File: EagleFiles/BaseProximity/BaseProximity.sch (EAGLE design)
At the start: 22 parts, among them Q3 2N3904

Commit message: board order for v1.0
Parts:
- added Q1: 2N3904, SparkFun-DiscreteSemi:TRANSISTOR_NPN2N3904-EZ
- added R1: 1K, SparkFun-Resistors:1KOHM-1/4W-1%(PTH)HORIZ-KIT
- renumbered 5983 to COMPASS, JP7 to TO_MBOT
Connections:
- new net IR_GND2: FRONTRIGHT.2, Q1.C, REAR.2, REARRIGHT.2, RIGHT.2
- new net N$1: Q1.B, R1.1
- net GND: now also Q1.E
- net GPIO12: now also R1.2
- net IR_GND: no longer FRONTRIGHT.2, REAR.2, REARRIGHT.2, RIGHT.2
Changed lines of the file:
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@@
 <part name="GPIO5" library="pinhead" deviceset="PINHD-1X3" device=""/>
 <part name="GPIO6" library="pinhead" deviceset="PINHD-1X3" device=""/>
-<part name="5983" library="pinhead" deviceset="PINHD-1X6" device=""/>
+<part name="COMPASS" library="pinhead" deviceset="PINHD-1X6" device=""/>
 <part name="GPIO13" library="pinhead" deviceset="PINHD-1X3" device=""/>
 <part name="GPIO19" library="pinhead" deviceset="PINHD-1X3" device=""/>
-<part name="JP7" library="pinhead" deviceset="PINHD-1X4" device=""/>
+<part name="TO_MBOT" library="pinhead" deviceset="PINHD-1X4" device=""/>
 <part name="Q3" library="SparkFun-DiscreteSemi" deviceset="TRANSISTOR_NPN" device="2N3904-EZ" value="2N3904"/>
 <part name="R5" library="SparkFun-Resistors" deviceset="1KOHM-1/4W-1%(PTH)" device="HORIZ-KIT" value="1K"/>
+<part name="Q1" library="SparkFun-DiscreteSemi" deviceset="TRANSISTOR_NPN" device="2N3904-EZ" value="2N3904"/>
+<part name="R1" library="SparkFun-Resistors" deviceset="1KOHM-1/4W-1%(PTH)" device="HORIZ-KIT" value="1K"/>
 </parts>
 <sheets>
@@
 <instance part="GPIO5" gate="A" x="114.3" y="170.18"/>
 <instance part="GPIO6" gate="A" x="114.3" y="154.94"/>
-<instance part="5983" gate="A" x="124.46" y="119.38"/>
+<instance part="COMPASS" gate="A" x="124.46" y="119.38"/>
 <instance part="GPIO13" gate="A" x="142.24" y="170.18"/>
 <instance part="GPIO19" gate="A" x="142.24" y="154.94"/>
-<instance part="JP7" gate="A" x="226.06" y="165.1"/>
+<instance part="TO_MBOT" gate="A" x="226.06" y="165.1"/>
 <instance part="Q3" gate="G$1" x="134.62" y="83.82"/>
 <instance part="R5" gate="G$1" x="124.46" y="83.82" rot="R180"/>
+<instance part="Q1" gate="G$1" x="78.74" y="111.76"/>
+<instance part="R1" gate="G$1" x="68.58" y="111.76" rot="R180"/>
 </instances>
 <busses>
@@
 </segment>
 <segment>
-<pinref part="5983" gate="A" pin="5"/>
+<pinref part="COMPASS" gate="A" pin="5"/>
 <wire x1="121.92" y1="116.84" x2="109.22" y2="116.84" width="0.1524" layer="91"/>
 <label x="109.22" y="116.84" size="1.778" layer="95"/>
@@
 </segment>
 <segment>
-<pinref part="JP7" gate="A" pin="4"/>
+<pinref part="TO_MBOT" gate="A" pin="4"/>
 <wire x1="223.52" y1="162.56" x2="208.28" y2="162.56" width="0.1524" layer="91"/>
 <label x="208.28" y="162.56" size="1.778" layer="95"/>
@@
 <label x="137.16" y="76.2" size="1.778" layer="95"/>
 </segment>
+<segment>
+<wire x1="81.28" y1="104.14" x2="81.28" y2="106.68" width="0.1524" layer="91"/>
+<pinref part="Q1" gate="G$1" pin="E"/>
+<label x="81.28" y="104.14" size="1.778" layer="95"/>
+</segment>
 </net>
 <net name="VCC" class="0">
@@
 </segment>
 <segment>
-<pinref part="5983" gate="A" pin="6"/>
+<pinref part="COMPASS" gate="A" pin="6"/>
 <wire x1="121.92" y1="114.3" x2="109.22" y2="114.3" width="0.1524" layer="91"/>
 <label x="109.22" y="114.3" size="1.778" layer="95"/>
@@
 </segment>
 <segment>
-<pinref part="5983" gate="A" pin="4"/>
+<pinref part="COMPASS" gate="A" pin="4"/>
 <wire x1="121.92" y1="119.38" x2="109.22" y2="119.38" width="0.1524" layer="91"/>
 <label x="109.22" y="119.38" size="1.778" layer="95"/>
@@
 </segment>
 <segment>
-<pinref part="5983" gate="A" pin="3"/>
+<pinref part="COMPASS" gate="A" pin="3"/>
 <wire x1="121.92" y1="121.92" x2="109.22" y2="121.92" width="0.1524" layer="91"/>
 <label x="109.22" y="121.92" size="1.778" layer="95"/>
@@
 </segment>
 <segment>
-<pinref part="JP7" gate="A" pin="1"/>
+<pinref part="TO_MBOT" gate="A" pin="1"/>
 <wire x1="223.52" y1="170.18" x2="208.28" y2="170.18" width="0.1524" layer="91"/>
 <label x="208.28" y="170.18" size="1.778" layer="95"/>
@@
 <net name="N$9" class="0">
 <segment>
-<pinref part="5983" gate="A" pin="2"/>
+<pinref part="COMPASS" gate="A" pin="2"/>
 <wire x1="121.92" y1="124.46" x2="109.22" y2="124.46" width="0.1524" layer="91"/>
 </segment>
@@
 <net name="N$12" class="0">
 <segment>
-<pinref part="5983" gate="A" pin="1"/>
+<pinref part="COMPASS" gate="A" pin="1"/>
 <wire x1="121.92" y1="127" x2="109.22" y2="127" width="0.1524" layer="91"/>
 </segment>
@@
 </segment>
 <segment>
-<pinref part="JP7" gate="A" pin="2"/>
+<pinref part="TO_MBOT" gate="A" pin="2"/>
 <wire x1="223.52" y1="167.64" x2="208.28" y2="167.64" width="0.1524" layer="91"/>
 <label x="208.28" y="167.64" size="1.778" layer="95"/>
@@
 </segment>
 <segment>
-<pinref part="JP7" gate="A" pin="3"/>
+<pinref part="TO_MBOT" gate="A" pin="3"/>
 <wire x1="223.52" y1="165.1" x2="208.28" y2="165.1" width="0.1524" layer="91"/>
 <label x="208.28" y="165.1" size="1.778" layer="95"/>
@@
 <wire x1="231.14" y1="81.28" x2="241.3" y2="81.28" width="0.1524" layer="91"/>
 <label x="236.22" y="81.28" size="1.778" layer="95"/>
+</segment>
+<segment>
+<pinref part="R1" gate="G$1" pin="2"/>
+<wire x1="63.5" y1="111.76" x2="60.96" y2="111.76" width="0.1524" layer="91"/>
+<label x="60.96" y="116.84" size="1.778" layer="95"/>
 </segment>
 </net>
@@
 </segment>
 <segment>
+<pinref part="LEFT" gate="A" pin="2"/>
+<wire x1="25.4" y1="38.1" x2="15.24" y2="38.1" width="0.1524" layer="91"/>
+<label x="15.24" y="38.1" size="1.778" layer="95"/>
+</segment>
+<segment>
+<pinref part="REARLEFT" gate="A" pin="2"/>
+<wire x1="25.4" y1="20.32" x2="17.78" y2="20.32" width="0.1524" layer="91"/>
+<label x="17.78" y="20.32" size="1.778" layer="95"/>
+</segment>
+<segment>
 <pinref part="FRONT" gate="A" pin="2"/>
 <wire x1="43.18" y1="55.88" x2="35.56" y2="55.88" width="0.1524" layer="91"/>
 <label x="35.56" y="55.88" size="1.778" layer="95"/>
 </segment>
+</net>
+<net name="N$1" class="0">
+<segment>
+<wire x1="73.66" y1="111.76" x2="76.2" y2="111.76" width="0.1524" layer="91"/>
+<pinref part="Q1" gate="G$1" pin="B"/>
+<pinref part="R1" gate="G$1" pin="1"/>
+</segment>
+</net>
+<net name="IR_GND2" class="0">
+<segment>
+<pinref part="Q1" gate="G$1" pin="C"/>
+<wire x1="81.28" y1="116.84" x2="81.28" y2="124.46" width="0.1524" layer="91"/>
+<label x="81.28" y="121.92" size="1.778" layer="95"/>
+</segment>
+<segment>
+<pinref part="REARRIGHT" gate="A" pin="2"/>
+<wire x1="60.96" y1="20.32" x2="53.34" y2="20.32" width="0.1524" layer="91"/>
+<label x="53.34" y="20.32" size="1.778" layer="95"/>
+</segment>
+<segment>
+<pinref part="RIGHT" gate="A" pin="2"/>
+<wire x1="60.96" y1="38.1" x2="53.34" y2="38.1" width="0.1524" layer="91"/>
+<label x="53.34" y="38.1" size="1.778" layer="95"/>
+</segment>
 <segment>
 <pinref part="FRONTRIGHT" gate="A" pin="2"/>
@@
 </segment>
 <segment>
-<pinref part="LEFT" gate="A" pin="2"/>
-<wire x1="25.4" y1="38.1" x2="15.24" y2="38.1" width="0.1524" layer="91"/>
-<label x="15.24" y="38.1" size="1.778" layer="95"/>
-</segment>
-<segment>
-<pinref part="REARLEFT" gate="A" pin="2"/>
-<wire x1="25.4" y1="20.32" x2="17.78" y2="20.32" width="0.1524" layer="91"/>
-<label x="17.78" y="20.32" size="1.778" layer="95"/>
-</segment>
-<segment>
 <pinref part="REAR" gate="A" pin="2"/>
 <wire x1="43.18" y1="20.32" x2="35.56" y2="20.32" width="0.1524" layer="91"/>
 <label x="35.56" y="20.32" size="1.778" layer="95"/>
 </segment>
-<segment>
-<pinref part="REARRIGHT" gate="A" pin="2"/>
-<wire x1="60.96" y1="20.32" x2="53.34" y2="20.32" width="0.1524" layer="91"/>
-<label x="53.34" y="20.32" size="1.778" layer="95"/>
-</segment>
-<segment>
-<pinref part="RIGHT" gate="A" pin="2"/>
-<wire x1="60.96" y1="38.1" x2="53.34" y2="38.1" width="0.1524" layer="91"/>
-<label x="53.34" y="38.1" size="1.778" layer="95"/>
-</segment>
-</net>
+</net>

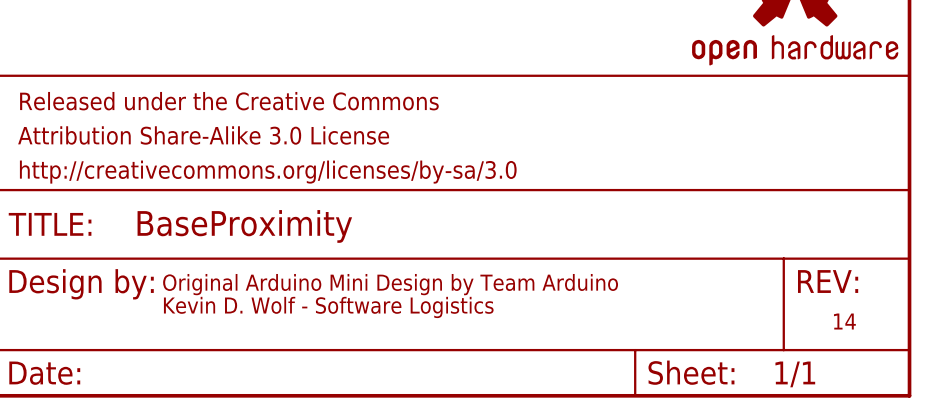
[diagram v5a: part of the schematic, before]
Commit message: update instructions for board
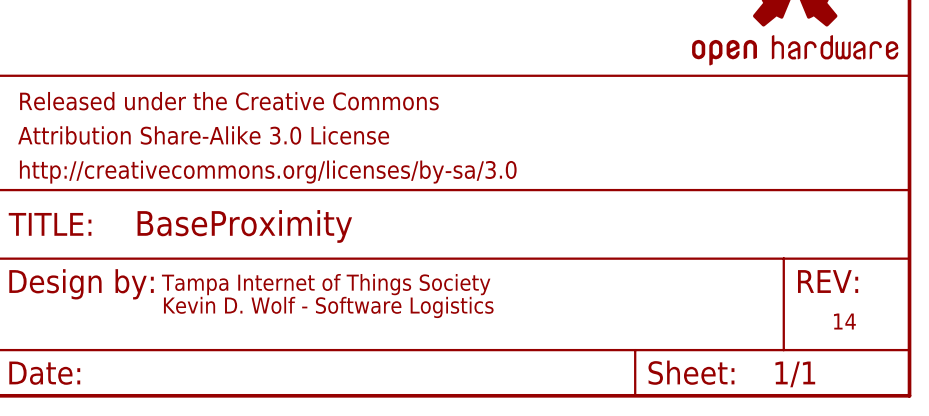
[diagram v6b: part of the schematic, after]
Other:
- note added: "Tampa Internet of Things Society"
- note removed: "Original Arduino Mini Design by Team Arduino"
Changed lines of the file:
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@@
 <sheet>
 <plain>
-<text x="165.862" y="11.684" size="1.778" layer="94">Original Arduino Mini Design by Team Arduino</text>
+<text x="165.862" y="11.684" size="1.778" layer="94">Tampa Internet of Things Society</text>
 <text x="165.862" y="9.144" size="1.778" layer="94">Kevin D. Wolf - Software Logistics</text>
 <text x="240.284" y="7.366" size="1.778" layer="94">14</text>

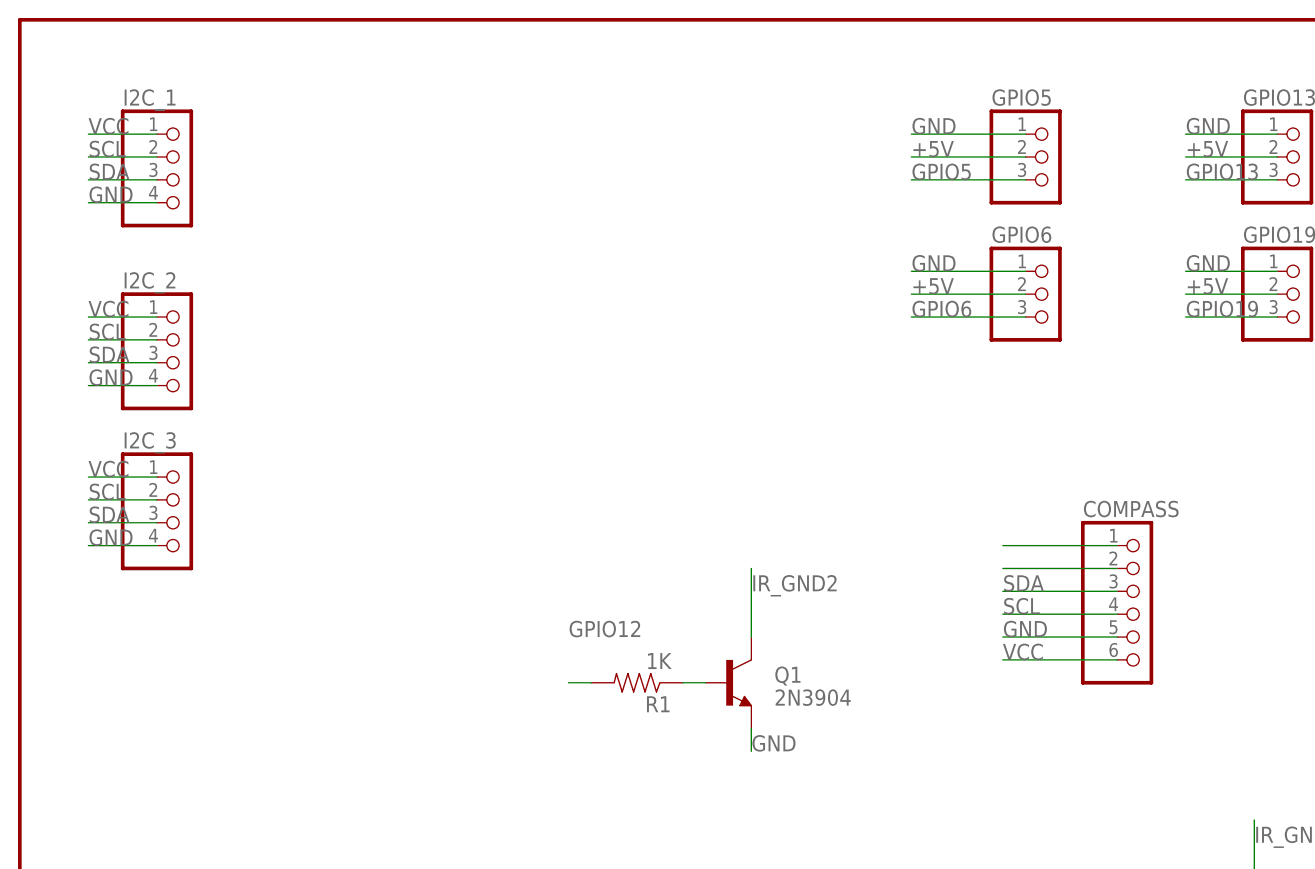
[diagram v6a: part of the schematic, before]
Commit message: updated board for new order
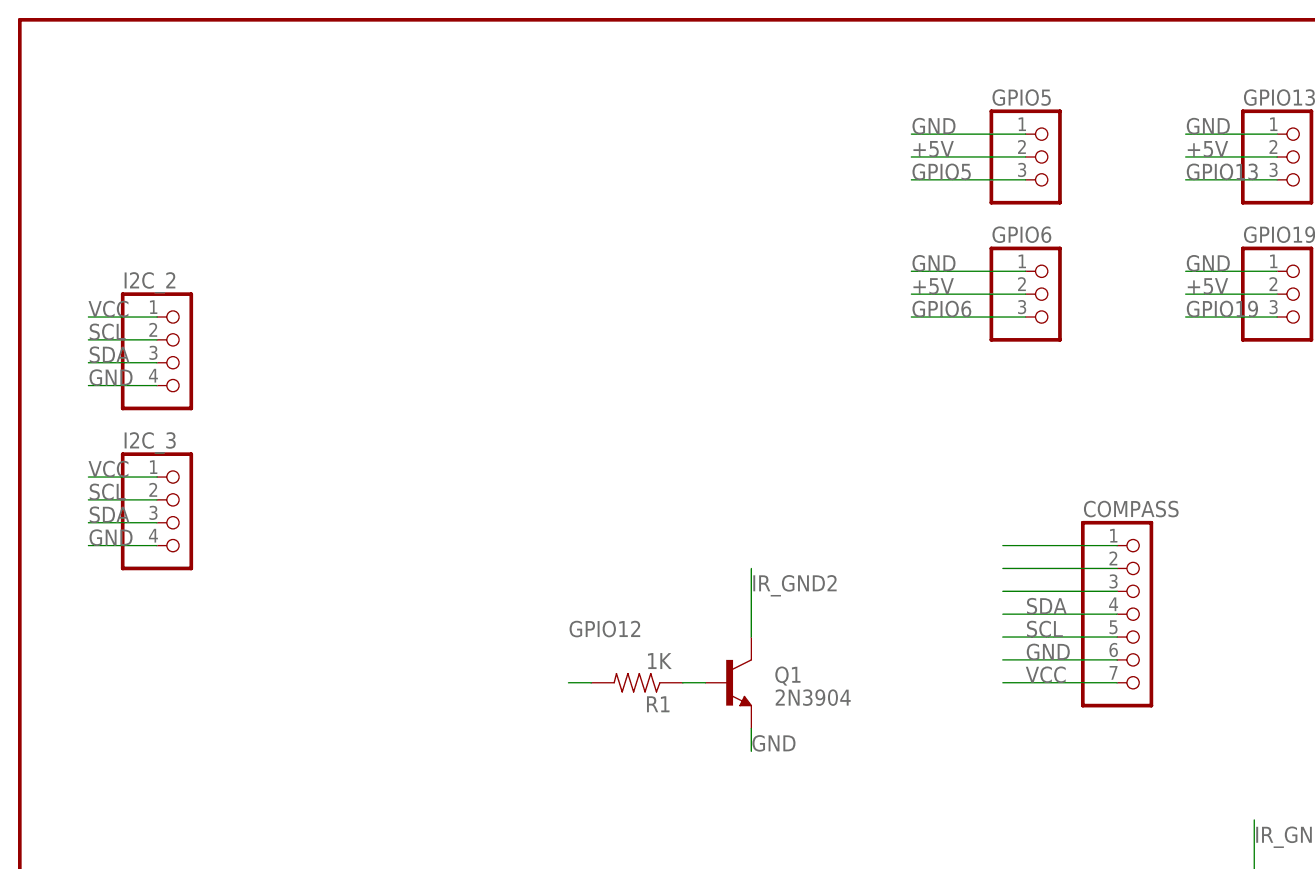
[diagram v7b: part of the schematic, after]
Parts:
- removed I2C_1: (no value), pinhead:PINHD-1X4
- COMPASS: device pinhead:PINHD-1X6 -> pinhead:PINHD-1X7
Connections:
- new net N$5: COMPASS.3
- net GND: now also COMPASS.6; no longer COMPASS.5, I2C_1.4
- net SCL: now also COMPASS.5; no longer COMPASS.4, I2C_1.2
- net SDA: now also COMPASS.4; no longer COMPASS.3, I2C_1.3
- net VCC: now also COMPASS.7; no longer COMPASS.6, I2C_1.1
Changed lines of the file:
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@@
 <?xml version="1.0" encoding="utf-8"?>
 <!DOCTYPE eagle SYSTEM "eagle.dtd">
-<eagle version="8.0.2">
+<eagle version="8.1.0">
 <drawing>
 <settings>
@@
 <part name="RIGHT" library="pinhead" deviceset="PINHD-1X3" device=""/>
 <part name="I2C_2" library="pinhead" deviceset="PINHD-1X4" device=""/>
-<part name="I2C_1" library="pinhead" deviceset="PINHD-1X4" device=""/>
 <part name="I2C_3" library="pinhead" deviceset="PINHD-1X4" device=""/>
 <part name="GPIO5" library="pinhead" deviceset="PINHD-1X3" device=""/>
 <part name="GPIO6" library="pinhead" deviceset="PINHD-1X3" device=""/>
-<part name="COMPASS" library="pinhead" deviceset="PINHD-1X6" device=""/>
+<part name="COMPASS" library="pinhead" deviceset="PINHD-1X7" device=""/>
 <part name="GPIO13" library="pinhead" deviceset="PINHD-1X3" device=""/>
 <part name="GPIO19" library="pinhead" deviceset="PINHD-1X3" device=""/>
@@
 <instance part="RIGHT" gate="A" x="63.5" y="38.1"/>
 <instance part="I2C_2" gate="A" x="17.78" y="147.32"/>
-<instance part="I2C_1" gate="A" x="17.78" y="167.64"/>
 <instance part="I2C_3" gate="A" x="17.78" y="129.54"/>
 <instance part="GPIO5" gate="A" x="114.3" y="170.18"/>
@@
 </segment>
 <segment>
-<pinref part="COMPASS" gate="A" pin="5"/>
-<wire x1="121.92" y1="116.84" x2="109.22" y2="116.84" width="0.1524" layer="91"/>
-<label x="109.22" y="116.84" size="1.778" layer="95"/>
-</segment>
-<segment>
-<pinref part="I2C_1" gate="A" pin="4"/>
-<wire x1="15.24" y1="165.1" x2="7.62" y2="165.1" width="0.1524" layer="91"/>
-<label x="7.62" y="165.1" size="1.778" layer="95"/>
-</segment>
-<segment>
 <pinref part="JP2" gate="A" pin="9"/>
 <wire x1="223.52" y1="109.22" x2="213.36" y2="109.22" width="0.1524" layer="91"/>
@@
 <label x="81.28" y="104.14" size="1.778" layer="95"/>
 </segment>
+<segment>
+<pinref part="COMPASS" gate="A" pin="6"/>
+<wire x1="121.92" y1="114.3" x2="109.22" y2="114.3" width="0.1524" layer="91"/>
+<label x="111.76" y="114.3" size="1.778" layer="95"/>
+</segment>
 </net>
 <net name="VCC" class="0">
@@
 </segment>
 <segment>
-<pinref part="COMPASS" gate="A" pin="6"/>
-<wire x1="121.92" y1="114.3" x2="109.22" y2="114.3" width="0.1524" layer="91"/>
-<label x="109.22" y="114.3" size="1.778" layer="95"/>
-</segment>
-<segment>
-<pinref part="I2C_1" gate="A" pin="1"/>
-<wire x1="15.24" y1="172.72" x2="7.62" y2="172.72" width="0.1524" layer="91"/>
-<label x="7.62" y="172.72" size="1.778" layer="95"/>
-</segment>
-<segment>
 <pinref part="I2C_2" gate="A" pin="1"/>
 <wire x1="15.24" y1="152.4" x2="7.62" y2="152.4" width="0.1524" layer="91"/>
@@
 <label x="7.62" y="134.62" size="1.778" layer="95"/>
 </segment>
+<segment>
+<pinref part="COMPASS" gate="A" pin="7"/>
+<wire x1="121.92" y1="111.76" x2="109.22" y2="111.76" width="0.1524" layer="91"/>
+<label x="111.76" y="111.76" size="1.778" layer="95"/>
+</segment>
 </net>
 <net name="SCL" class="0">
@@
 </segment>
 <segment>
-<pinref part="COMPASS" gate="A" pin="4"/>
-<wire x1="121.92" y1="119.38" x2="109.22" y2="119.38" width="0.1524" layer="91"/>
-<label x="109.22" y="119.38" size="1.778" layer="95"/>
-</segment>
-<segment>
-<pinref part="I2C_1" gate="A" pin="2"/>
-<wire x1="15.24" y1="170.18" x2="7.62" y2="170.18" width="0.1524" layer="91"/>
-<label x="7.62" y="170.18" size="1.778" layer="95"/>
-</segment>
-<segment>
 <pinref part="I2C_2" gate="A" pin="2"/>
 <wire x1="15.24" y1="149.86" x2="7.62" y2="149.86" width="0.1524" layer="91"/>
@@
 <label x="7.62" y="132.08" size="1.778" layer="95"/>
 </segment>
+<segment>
+<pinref part="COMPASS" gate="A" pin="5"/>
+<wire x1="121.92" y1="116.84" x2="109.22" y2="116.84" width="0.1524" layer="91"/>
+<label x="111.76" y="116.84" size="1.778" layer="95"/>
+</segment>
 </net>
 <net name="SDA" class="0">
@@
 </segment>
 <segment>
-<pinref part="COMPASS" gate="A" pin="3"/>
-<wire x1="121.92" y1="121.92" x2="109.22" y2="121.92" width="0.1524" layer="91"/>
-<label x="109.22" y="121.92" size="1.778" layer="95"/>
-</segment>
-<segment>
-<pinref part="I2C_1" gate="A" pin="3"/>
-<wire x1="15.24" y1="167.64" x2="7.62" y2="167.64" width="0.1524" layer="91"/>
-<label x="7.62" y="167.64" size="1.778" layer="95"/>
-</segment>
-<segment>
 <pinref part="I2C_2" gate="A" pin="3"/>
 <wire x1="15.24" y1="147.32" x2="7.62" y2="147.32" width="0.1524" layer="91"/>
@@
 <wire x1="15.24" y1="129.54" x2="7.62" y2="129.54" width="0.1524" layer="91"/>
 <label x="7.62" y="129.54" size="1.778" layer="95"/>
+</segment>
+<segment>
+<pinref part="COMPASS" gate="A" pin="4"/>
+<wire x1="121.92" y1="119.38" x2="109.22" y2="119.38" width="0.1524" layer="91"/>
+<label x="111.76" y="119.38" size="1.778" layer="95"/>
 </segment>
 </net>
@@
 </segment>
 </net>
+<net name="N$5" class="0">
+<segment>
+<pinref part="COMPASS" gate="A" pin="3"/>
+<wire x1="121.92" y1="121.92" x2="109.22" y2="121.92" width="0.1524" layer="91"/>
+</segment>
+</net>
